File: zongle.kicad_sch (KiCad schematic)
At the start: 13 parts

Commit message: draft of layout
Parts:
- removed U?: SRV05-4, PCM_marbastlib-various:SOT-23-6-routable, symbol marbastlib-various:SRV05-4
- added U2: TPD2EUSB30, Package_TO_SOT_SMD:Texas_DRT-3, symbol Power_Protection:TPD2EUSB30
- J1: renamed from J?; footprint (none) -> Connector_USB:USB_C_Plug_JAE_DX07P024AJ1
- J2: renamed from J?; footprint PCM_marbastlib-various:CON_TC2030_outlined -> marbastlib-various:CON_TC2030_outlined
- SWReset1: renamed from SWReset; footprint (none) -> Button_Switch_SMD:SW_Tactile_SPST_NO_Straight_CK_PTS636Sx25SMTRLFS
- gave numbers to parts that had none: 1
- renumbered ... to ...1, TP3V to TP3V1, TPD+ to TPD+1, TPGND to TPGND1
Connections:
- net D+: now also U2.1 (D+)
- net D-: now also U2.2 (D-)
- net GND: now also U2.3 (GND)
- no-connect marks 36 -> 34
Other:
- note added: "Make sure all shield pins are tied to gnd find the slim plug footprint understand the integration"
- note removed: "Make sure all shield pins are tied to gnd"

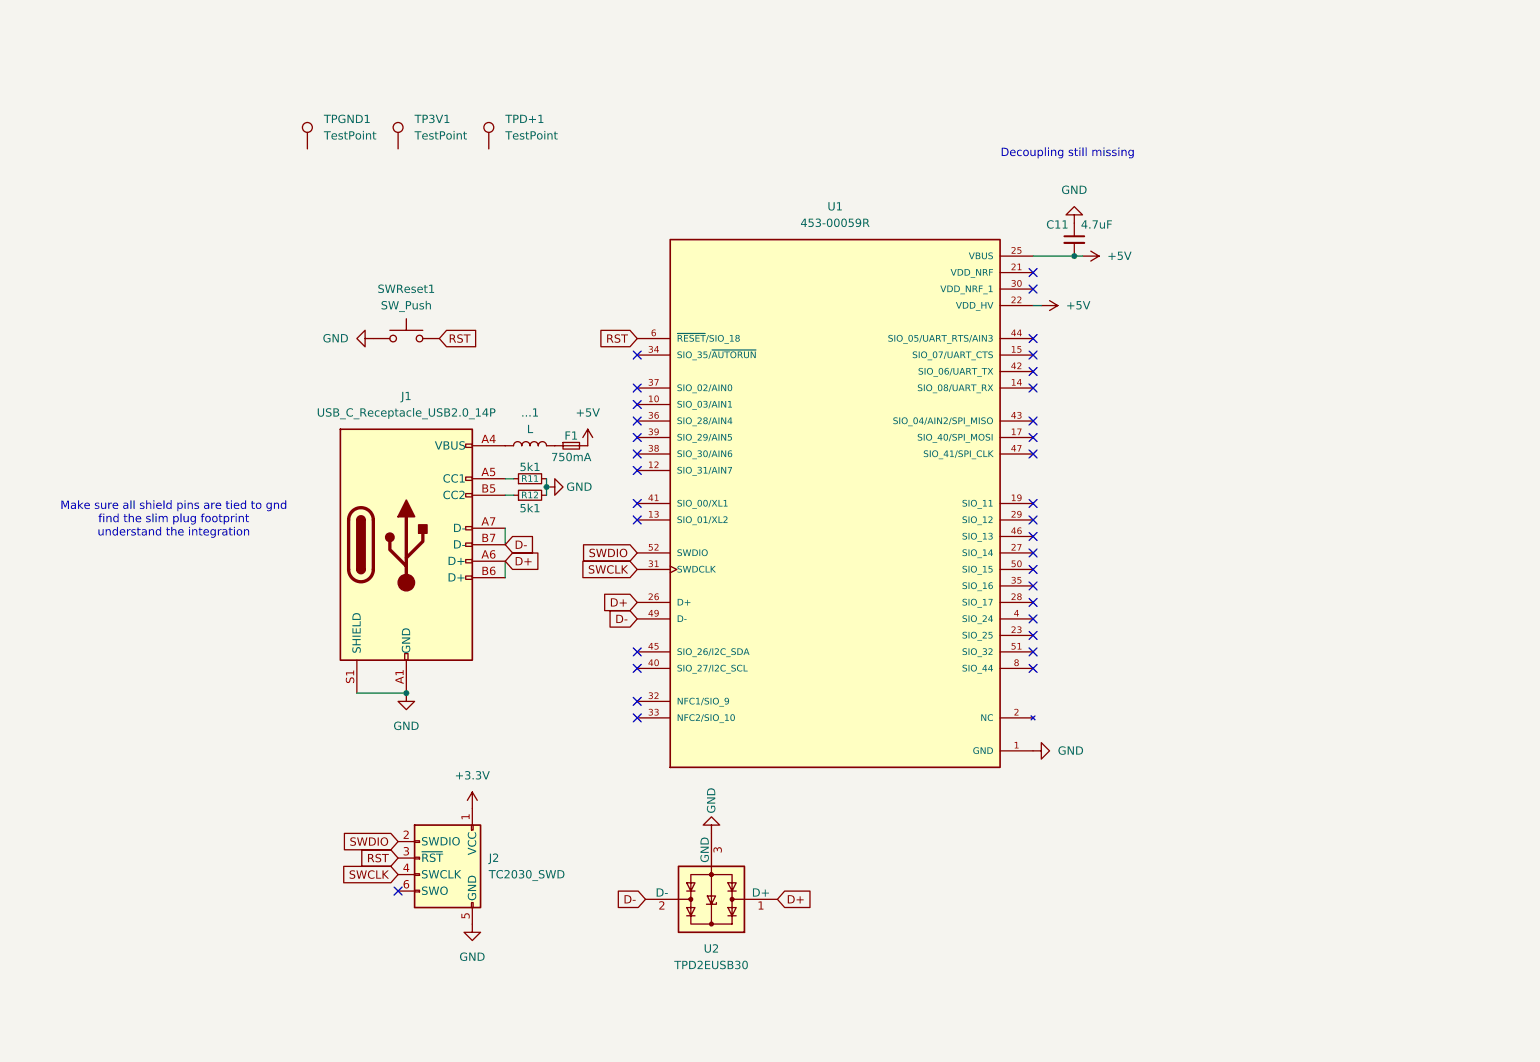
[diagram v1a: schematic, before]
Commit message: further routing. still missig footprints for testpoints and reset button, most of the routing is now done, will need some cleanup + drc fixesw
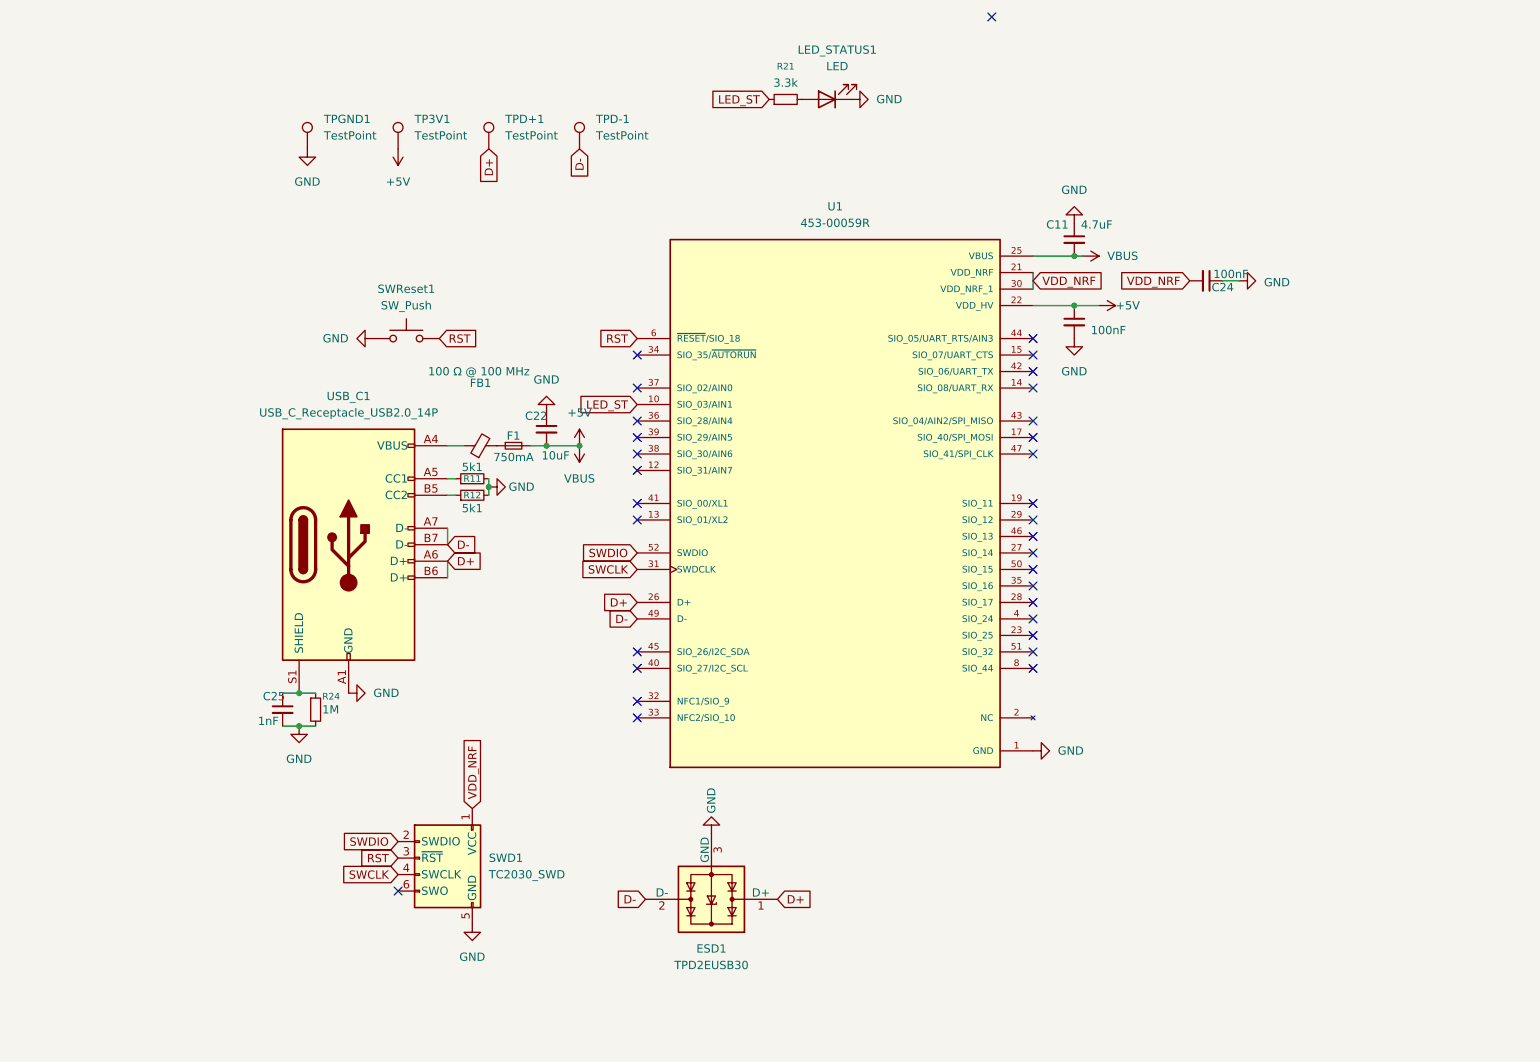
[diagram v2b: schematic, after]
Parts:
- removed ...1: L, symbol Device:L
- added C22: 10uF, Capacitor_SMD:C_0402_1005Metric, symbol Device:C_Small
- added C23, C24: 100nF, Capacitor_SMD:C_0402_1005Metric, symbol Device:C_Small
- added C25: 1nF, Capacitor_SMD:C_0402_1005Metric, symbol Device:C_Small
- added FB1: 100 Ω @ 100 MHz, Resistor_SMD:R_0402_1005Metric, symbol Device:FerriteBead_Small
- added LED_STATUS1: LED, LED_SMD:LED_0402_1005Metric, symbol Device:LED
- added R21: 3.3k, Resistor_SMD:R_0402_1005Metric, symbol Device:R_Small
- added R24: 1M, Resistor_SMD:R_0402_1005Metric, symbol Device:R_Small
- added TPD-1: TestPoint, TestPoint:TestPoint_Keystone_5000-5004_Miniature, symbol Connector:TestPoint
- C11: footprint (none) -> Capacitor_SMD:C_0402_1005Metric
- F1: footprint (none) -> Fuse:Fuse_0402_1005Metric
- R11, R12: footprint (none) -> Resistor_SMD:R_0402_1005Metric
- SWReset1: footprint Button_Switch_SMD:SW_Tactile_SPST_NO_Straight_CK_PTS636Sx25SMTRLFS -> Button_Switch_SMD:SW_SPST_EVQP2_MiddlePushTravel_H2.5mm
- TP3V1, TPD+1, TPGND1: footprint (none) -> TestPoint:TestPoint_Keystone_5000-5004_Miniature
- renumbered U2 to ESD1, J2 to SWD1, J1 to USB_C1
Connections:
- net +3.3V is gone; now on net VDD_NRF: SWD1.1 (VCC)
- net +5V: now also TP3V1.1, C22.2, C23.1
- net D+: now also TPD+1.1
- net D-: now also TPD-1.1
- net GND: now also TPGND1.1, C22.1, C23.2, C24.1, C25.2, LED_STATUS1.1 (K), R24.2; no longer USB_C1.S1 (SHIELD)
- net at USB_C1.A4 (VBUS), USB_C1.A9 (VBUS), USB_C1.B4 (VBUS)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: now also FB1.1
- net at F1.1: now also FB1.2
- net LED_ST: now reaches U1.10 (SIO_03/AIN1)
- net LED_ST: now also R21.1
- net VDD_NRF: now reaches U1.21 (VDD_NRF)
- net VDD_NRF: now also U1.30 (VDD_NRF_1), C24.2
- new net: LED_STATUS1.2 (A), R21.2
- new net: C25.1, R24.1, USB_C1.S1 (SHIELD)
- no-connect marks 34 -> 32
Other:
- note removed: "Decoupling still missing"
- note removed: "Make sure all shield pins are tied to gnd find the slim plug footprint understand the integration"
- moved on the sheet: F1, R11, R12, USB_C1

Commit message: used actual symbol of usb c port. redid routing. saved 2mm in length. fixed 3d model for usb c receptacle, now using 6 layers for cheap via in pad to avoid having to pay for microvias
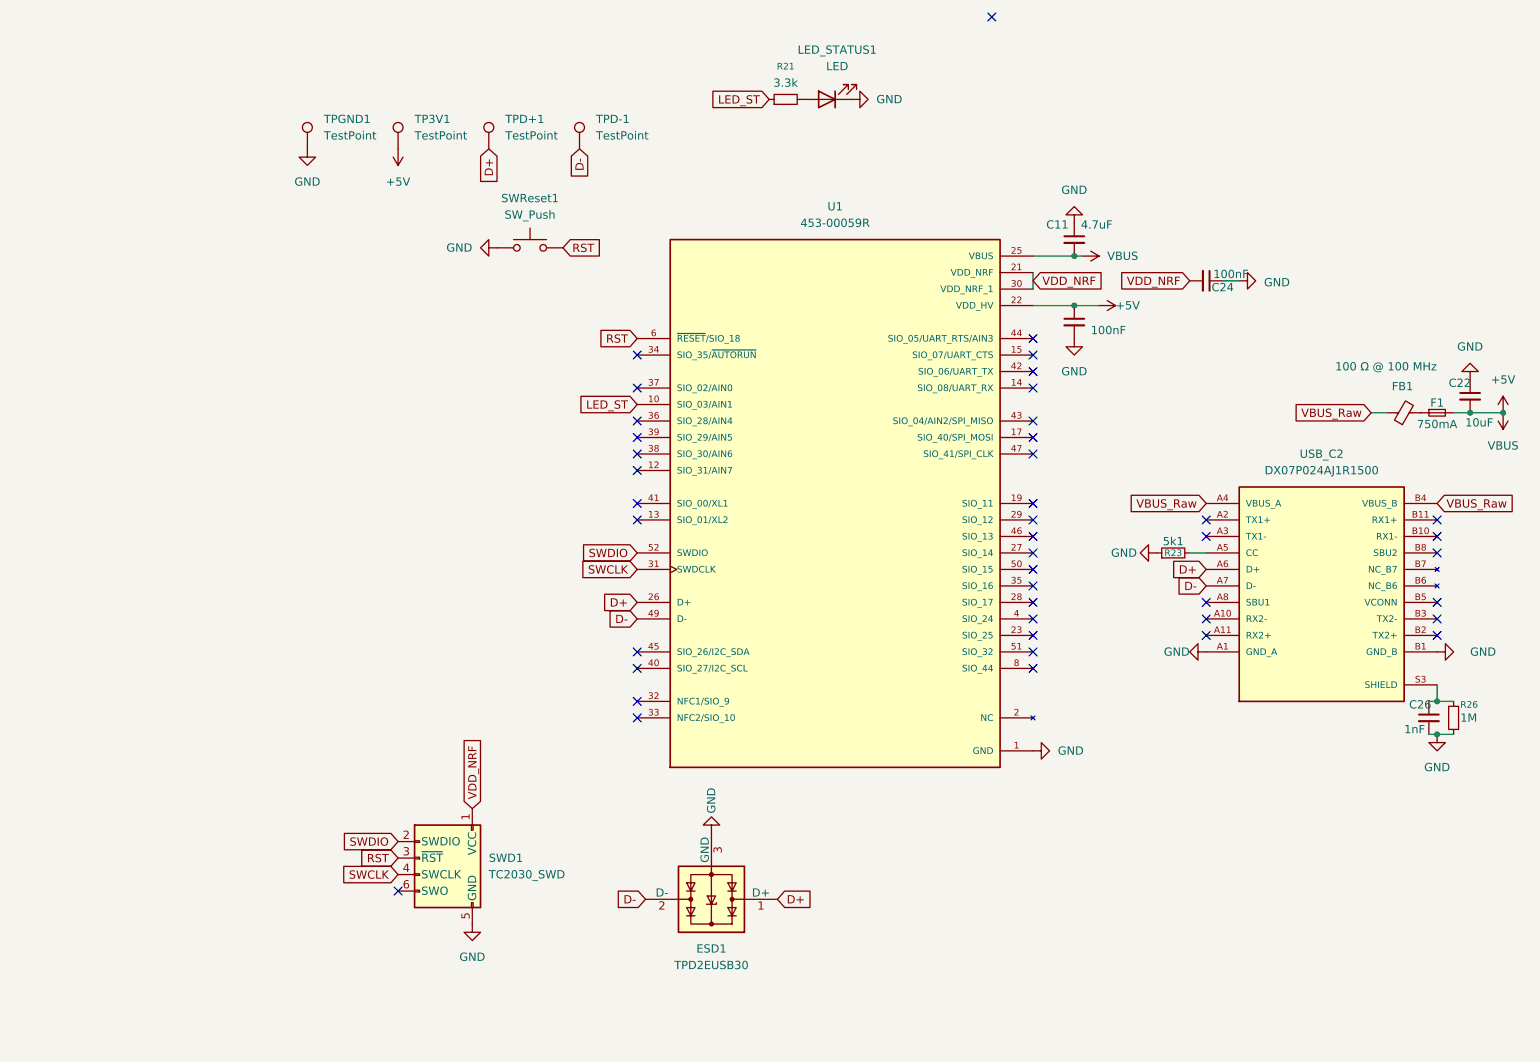
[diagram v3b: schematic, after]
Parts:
- removed C25: 1nF, Capacitor_SMD:C_0402_1005Metric, symbol Device:C_Small
- removed R11, R12: 5k1, Resistor_SMD:R_0402_1005Metric, symbol Device:R_Small
- removed R24: 1M, Resistor_SMD:R_0402_1005Metric, symbol Device:R_Small
- removed USB_C1: USB_C_Receptacle_USB2.0_14P, Connector_USB:USB_C_Plug_JAE_DX07P024AJ1, symbol Connector:USB_C_Receptacle_USB2.0_14P
- added C26: 1nF, Capacitor_SMD:C_0402_1005Metric, symbol Device:C_Small
- added R23: 5k1, Resistor_SMD:R_0402_1005Metric, symbol Device:R_Small
- added R26: 1M, Resistor_SMD:R_0402_1005Metric, symbol Device:R_Small
- added USB_C2: DX07P024AJ1R1500, USB_C_MALE_LONG:USB_C_MALE_LONG, symbol USB_C_MALE_LONG:DX07P024AJ1R1500
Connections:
- net D+: now also USB_C2.A6 (D+)
- net D-: now also USB_C2.A7 (D-)
- net GND: now also C26.2, R23.1, R26.2, USB_C2.A1 (GND_A), USB_C2.A12 (GND_A), USB_C2.B1 (GND_B), USB_C2.B12 (GND_B)
- net VBUS_A: now reaches FB1.1
- net VBUS_A: now also USB_C2.A4 (VBUS_A), USB_C2.A9 (VBUS_A), USB_C2.B4 (VBUS_B), USB_C2.B9 (VBUS_B)
- new net: C26.1, R26.1, USB_C2.S3 (SHIELD), USB_C2.S4 (SHIELD), USB_C2.S5 (SHIELD), USB_C2.S6 (SHIELD)
- new net: R23.2, USB_C2.A5 (CC)
- no-connect marks 32 -> 43
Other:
- moved on the sheet: C22, F1, FB1, SWReset1

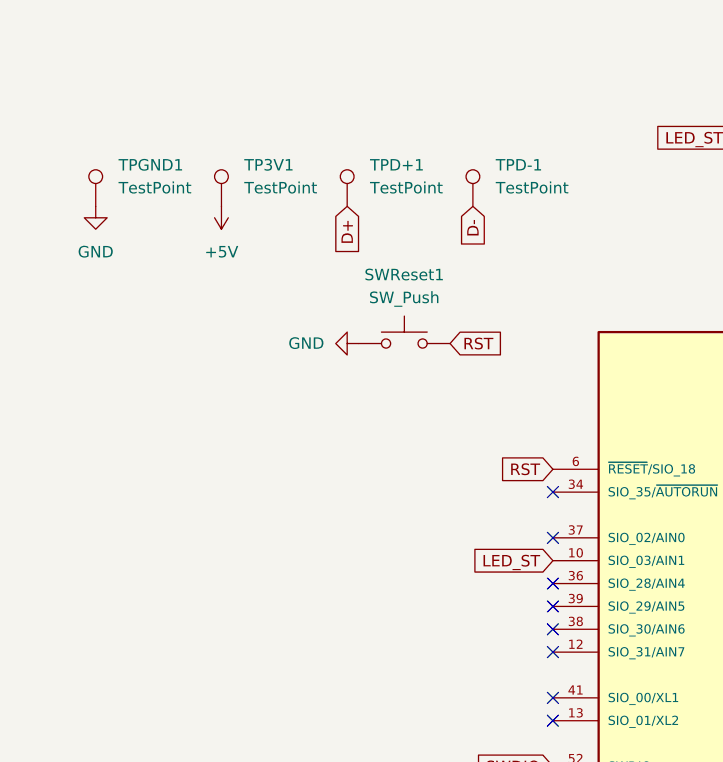
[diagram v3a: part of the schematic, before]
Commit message: some layout changes. fixed testpoint size. found fitting reset button. moved all parts to the top side, now missing part asignment
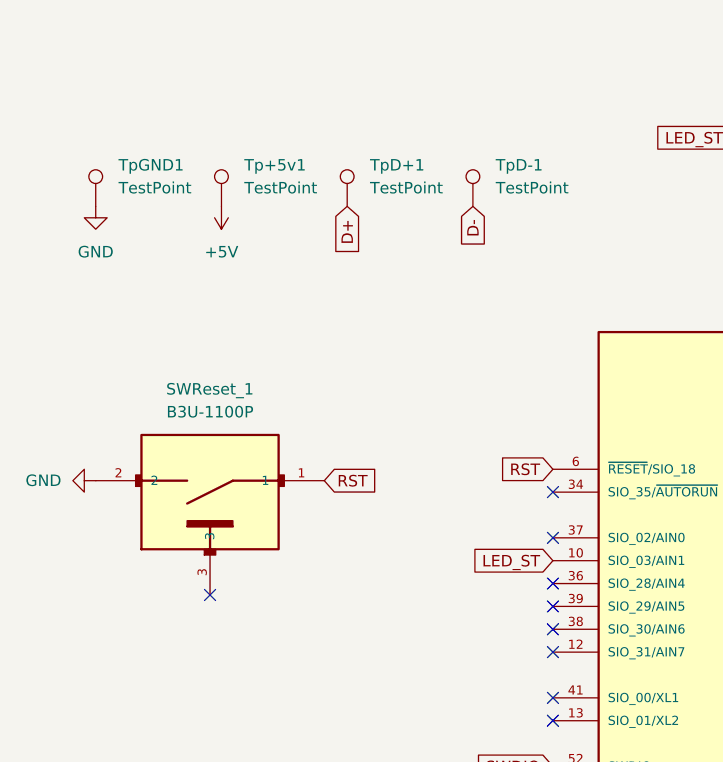
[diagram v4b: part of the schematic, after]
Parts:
- removed SWReset1: SW_Push, Button_Switch_SMD:SW_SPST_EVQP2_MiddlePushTravel_H2.5mm, symbol Switch:SW_Push
- added SWReset_1: B3U-1100P, Button_Switch_SMD:SW_SPST_B3U-1000P, symbol B3U-1100P:B3U-1100P
- Tp+5v1: renamed from TP3V1; footprint TestPoint:TestPoint_Keystone_5000-5004_Miniature -> TestPoint:TestPoint_Pad_1.0x1.0mm
- TpD+1: renamed from TPD+1; footprint TestPoint:TestPoint_Keystone_5000-5004_Miniature -> TestPoint:TestPoint_Pad_1.0x1.0mm
- TpD-1: renamed from TPD-1; footprint TestPoint:TestPoint_Keystone_5000-5004_Miniature -> TestPoint:TestPoint_Pad_1.0x1.0mm
- TpGND1: renamed from TPGND1; footprint TestPoint:TestPoint_Keystone_5000-5004_Miniature -> TestPoint:TestPoint_Pad_1.0x1.0mm
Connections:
- net GND: now also SWReset_1.2
- net RST: now also SWReset_1.1
- no-connect marks 43 -> 44
